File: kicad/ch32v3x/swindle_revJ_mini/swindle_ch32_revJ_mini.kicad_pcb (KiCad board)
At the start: 2 copper layers, 49.8 x 33.3 mm, 65 parts, among them J1 jtag, J10 Debug port, J2 Conn_01x03_Socket, J2_DFU1 con2, J3 Dbg, J4 USB, J5 Debug port, J6 Debug port, J7 Conn_01x03_Pin, J8 Debug port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

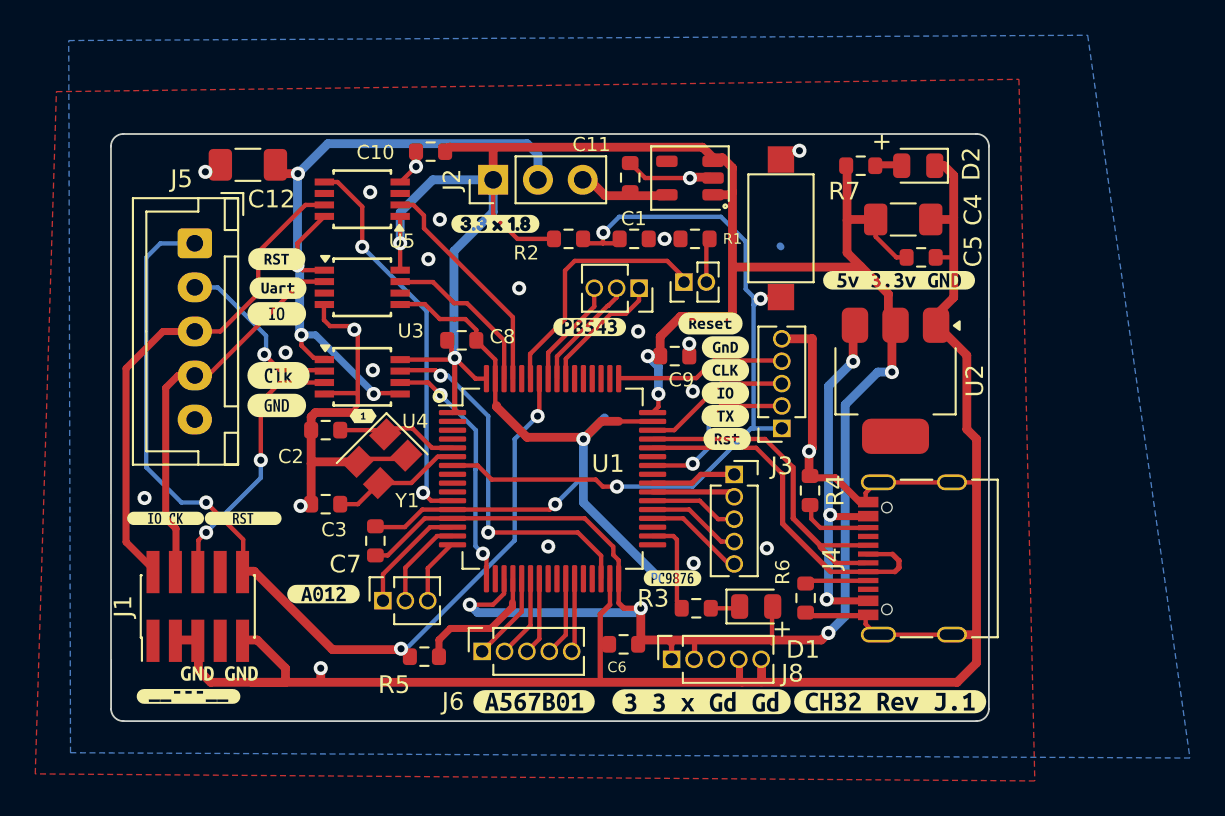
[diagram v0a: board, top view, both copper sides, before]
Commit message: add a WS2812b to the mini version, mini version for CH32,GD32 and RP2xxx
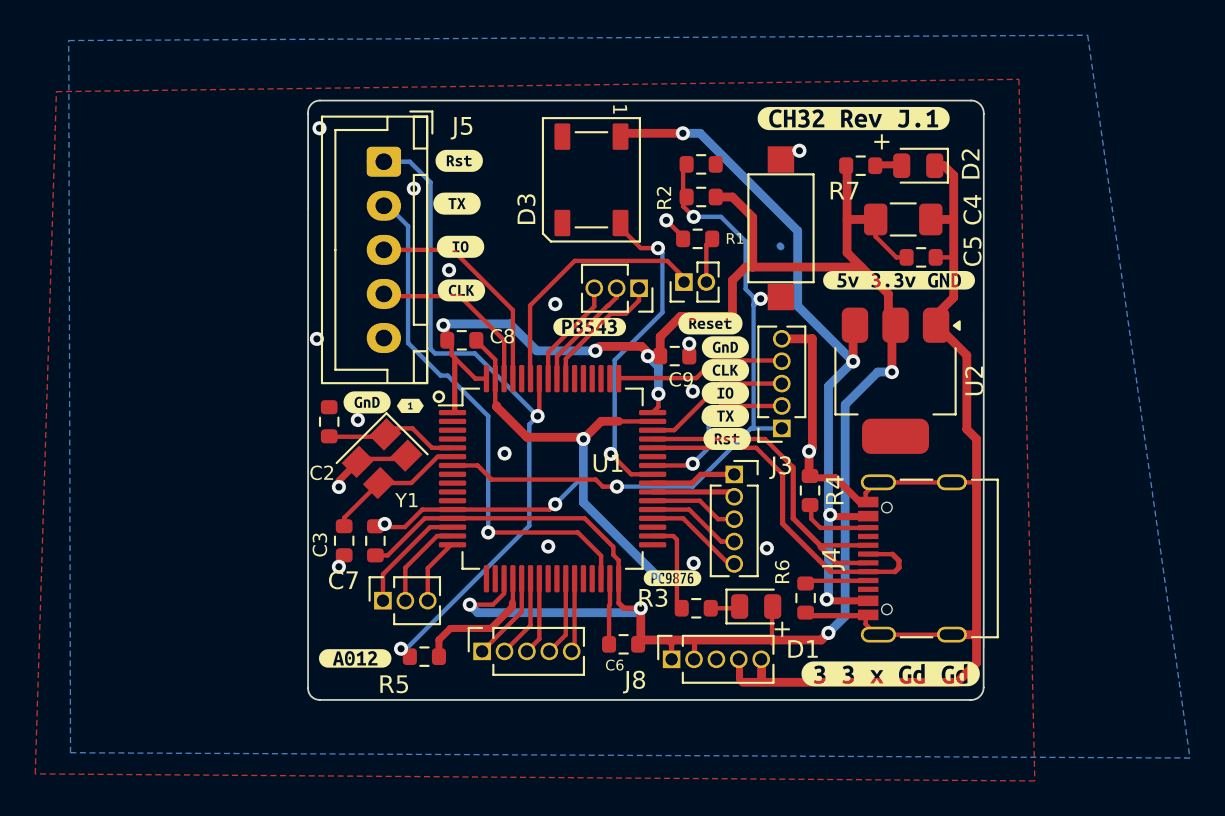
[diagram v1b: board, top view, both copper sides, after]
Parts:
- removed C10, C11: 100n, Resistor_SMD:R_0603_1608Metric
- removed C12: 100u, Capacitor_SMD:C_1206_3216Metric_Pad1.33x1.80mm_HandSolder
- removed J1: jtag, Connector_PinHeader_1.27mm:PinHeader_2x05_P1.27mm_Vertical_SMD
- removed J2: Conn_01x03_Socket, Connector_PinHeader_2.54mm:PinHeader_1x03_P2.54mm_Vertical
- removed U3: 3V->VTREF, Package_SO:TSSOP-8_3x3mm_P0.65mm
- removed U4: VTREF->3V, Package_SO:TSSOP-8_3x3mm_P0.65mm
- removed U5: VTREF<->3V, Package_SO:TSSOP-8_3x3mm_P0.65mm
- removed U6: RT9013-33GB, PCM_Package_TO_SOT_SMD_AKL:TSOT-23-5
- removed kibuzzard-66C04372: G***, kibuzzard-66C04372
- removed kibuzzard-66C0437E: G***, kibuzzard-66C0437E
- removed kibuzzard-67135DB6: G***, kibuzzard-67135DB6
- removed kibuzzard-67137B47: G***, kibuzzard-67137B47
- removed kibuzzard-67137B7B: G***, kibuzzard-67137B7B
- removed kibuzzard-6713DC16: G***, kibuzzard-6713DC16
- removed kibuzzard-6713DC2E: G***, kibuzzard-6713DC2E
- removed kibuzzard-6714FCCA: G***, kibuzzard-6714FCCA
- removed kibuzzard-6714FD27: G***, kibuzzard-6714FD27
- removed kibuzzard-6731069B: G***, kibuzzard-6731069B
- removed kibuzzard-67310708: G***, kibuzzard-67310708
- removed kibuzzard-6731071F: G***, kibuzzard-6731071F
- added D3: WS2812B, LED_SMD:LED_WS2812B_PLCC4_5.0x5.0mm_P3.2mm, F.Cu at (132.8, 69.5)
- added kibuzzard-65C1C789: G***, kibuzzard-65C1C789, F.Cu at (120.0, 82.1)
- added kibuzzard-65C1C8EE: G***, kibuzzard-65C1C8EE, F.Cu at (125.4, 75.8)
- added kibuzzard-65C1C918: G***, kibuzzard-65C1C918, F.Cu at (125.3, 73.3)
- added kibuzzard-65C1C92F: G***, kibuzzard-65C1C92F, F.Cu at (125.1, 70.8)
- added kibuzzard-65C1C972: G***, kibuzzard-65C1C972, F.Cu at (125.3, 68.4)
- moved kibuzzard-6869421E 33.1 mm to (147.6, 66.0)
- moved J5 11.7 mm to (121.0, 68.5)
- moved kibuzzard-6714FD4B 10.8 mm to (149.7, 97.5)
- moved R2 7.89 mm to (139.0, 70.5), turned to 180 degrees
- moved C1 5.68 mm to (139.0, 68.6)
- moved kibuzzard-67135D9A 4.07 mm to (119.4, 96.6)
- moved kibuzzard-671361D3 2.74 mm to (122.5, 82.3)
- moved C3 2.33 mm to (118.7, 90.0), turned to -90 degrees
- moved C2 0.52 mm to (117.9, 83.2), turned to 90 degrees
- moved R1 0.15 mm to (138.8, 72.8)
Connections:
- net Net-(U2-VI) renamed VBUS
- U1 pad 17: INOUT_SWO_3v -> INOUT_SWO
- U1 pad 30: OUT_UART_RX_3V -> OUT_UART_RX
- U1 pad 41: unconnected-(U1-PA8-Pad41) -> PA8
- U1 pad 61: OUT_SWDIO_3V -> OUT_SWDIO
- U1 pad 62: OUT_SWDCLK_3V -> OUT_SWDCLK
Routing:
- net GND: track 200.5 -> 126.3 mm, vias 24 -> 20
- net VTREF: track 40.3 -> 0.00 mm, vias 4 -> 0
- net +3.3V: track 163.6 -> 126.9 mm
- net SWIO_DIR_3V: track 22.5 -> 0.00 mm, vias 2 -> 0
- net OUT_UART_RX_3V: track 21.1 -> 0.00 mm, vias 2 -> 0
- net VBUS: track 20.5 -> 41.4 mm, vias 3 -> 4
- net OUT_UART_RX: track 10.4 -> 29.1 mm
- net PA8: track 0.00 -> 18.4 mm, vias 0 -> 2
- net OUT_SWDIO: track 28.9 -> 12.6 mm
- net INOUT_SWO: track 15.4 -> 0.00 mm, vias 2 -> 0
- net INOUT_SWO_3v: track 14.4 -> 0.00 mm, vias 2 -> 0
- net INOUT_NRESET: track 53.6 -> 39.8 mm, vias 3 -> 2
- net OUT_SWDIO_3V: track 12.9 -> 0.00 mm
- net OUT_SWDCLK: track 22.1 -> 9.91 mm
- net OUT_SWDCLK_3V: track 9.50 -> 0.00 mm
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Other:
- board size 49.8 x 33.3 mm -> 38.3 x 34 mm

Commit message: kicad: order to pcbway
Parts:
- added C10: 100n, Resistor_SMD:R_0603_1608Metric, F.Cu at (136.6, 68.0)
- added Q1: DMG2302U, Package_TO_SOT_SMD:SOT-23, F.Cu at (127.9, 67.5)
- added R8: 330, Resistor_SMD:R_0603_1608Metric, F.Cu at (125.0, 67.0)
- added R9: 1k, Resistor_SMD:R_0603_1608Metric, F.Cu at (128.6, 72.4)
- moved kibuzzard-65C1C972 1.62 mm to (125.3, 70.0)
- moved kibuzzard-65C1C92F 1.43 mm to (125.3, 72.3)
- moved kibuzzard-65C1C918 0.25 mm to (125.4, 73.5)
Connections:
- D3 pad 4: PA8 -> PB4
- U1 pad 58: INOUT_NRESET -> DRIVE_RESET
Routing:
- net PA8: track 18.4 -> 0.00 mm, vias 2 -> 0
- net DRIVE_RESET: track 0.00 -> 13.8 mm, vias 0 -> 2
- net PB4: track 6.55 -> 12.7 mm, vias 0 -> 1
- net Net-(Q1-D): track 0.00 -> 3.02 mm
- net INOUT_NRESET: track 39.8 -> 41.9 mm, vias 2 -> 1
- net GND: track 126.3 -> 127.1 mm, vias 20 -> 21

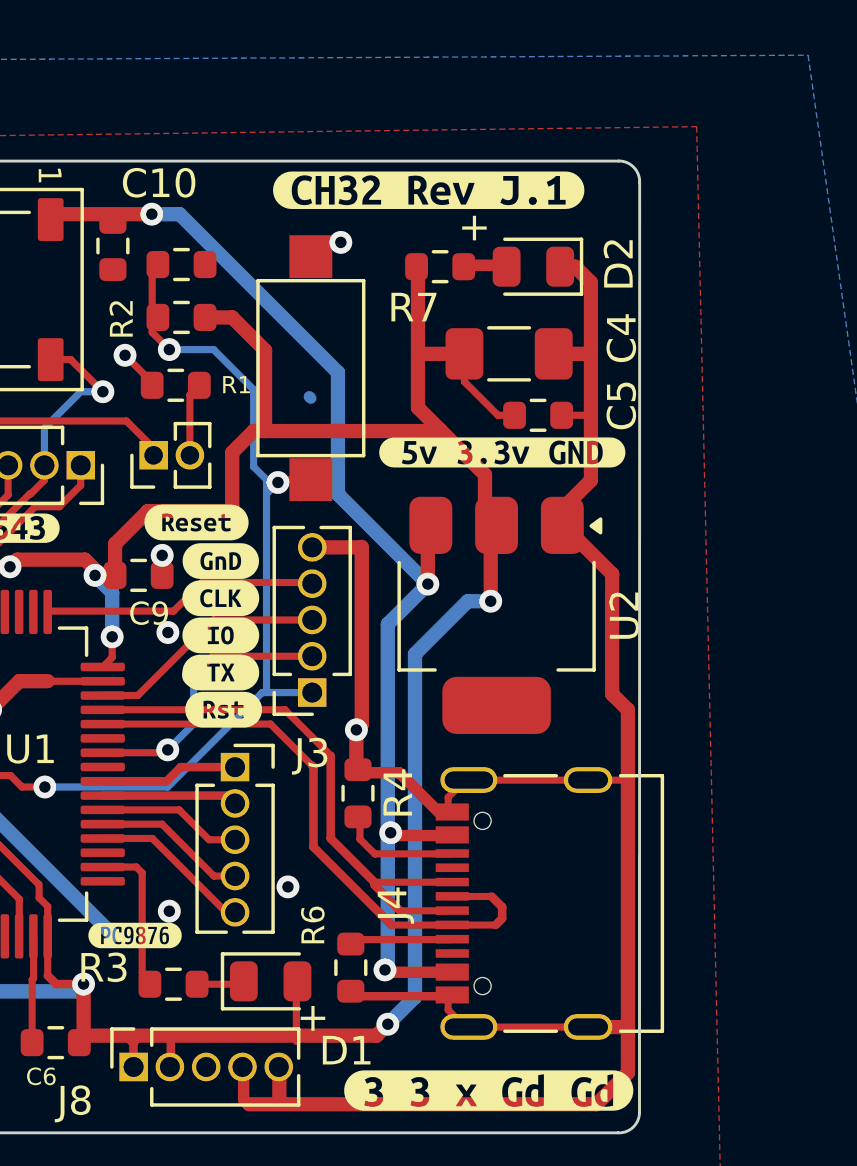
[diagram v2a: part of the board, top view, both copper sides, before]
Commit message: Kicad : ch32v3, add a (optional) 1.2k pullup on D+ so it can be used for GD32F303/64pins package
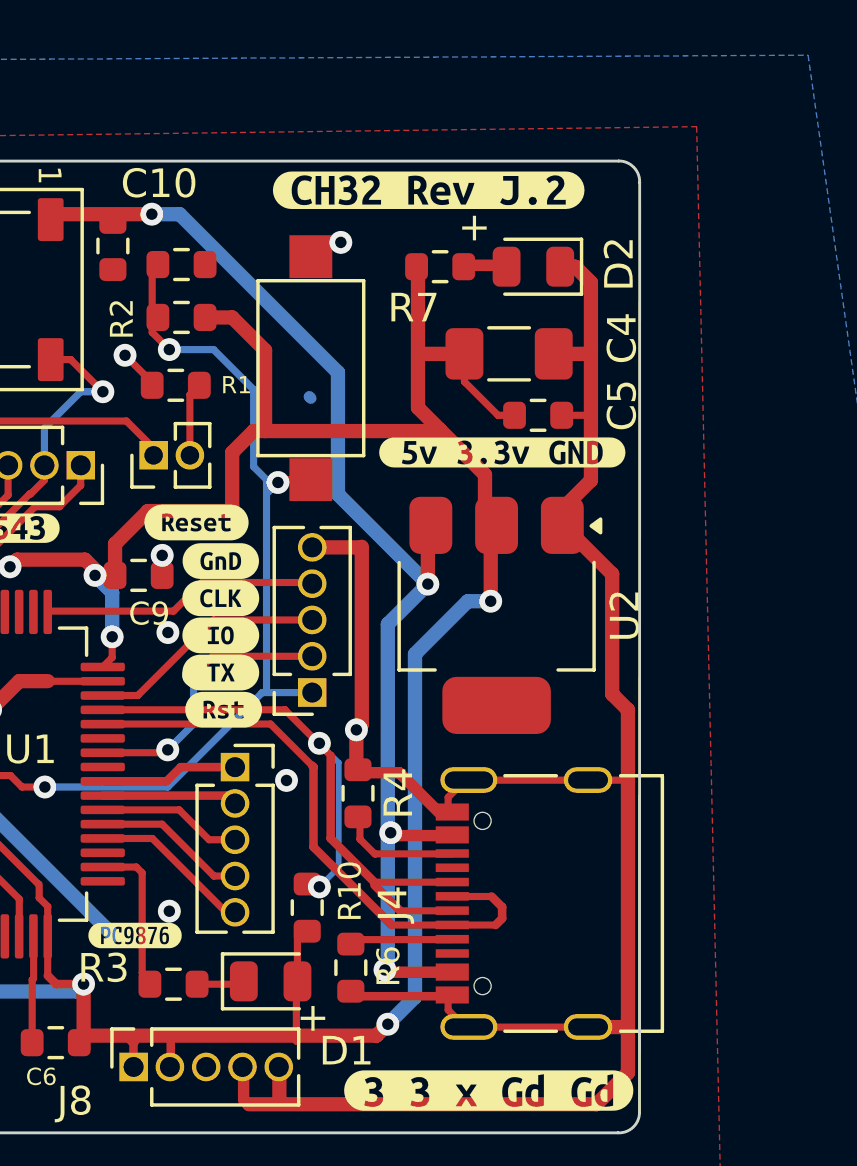
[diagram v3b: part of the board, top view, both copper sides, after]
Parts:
- removed kibuzzard-6869421E: G***, kibuzzard-6869421E
- added R10: 1.2k, Resistor_SMD:R_0603_1608Metric, F.Cu at (143.4, 91.1)
- added kibuzzard-68977CD7: G***, kibuzzard-68977CD7, F.Cu at (147.6, 66.0)
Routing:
- net D+: track 19.3 -> 24.9 mm, vias 0 -> 2
- net +3.3V: track 126.9 -> 129.0 mm

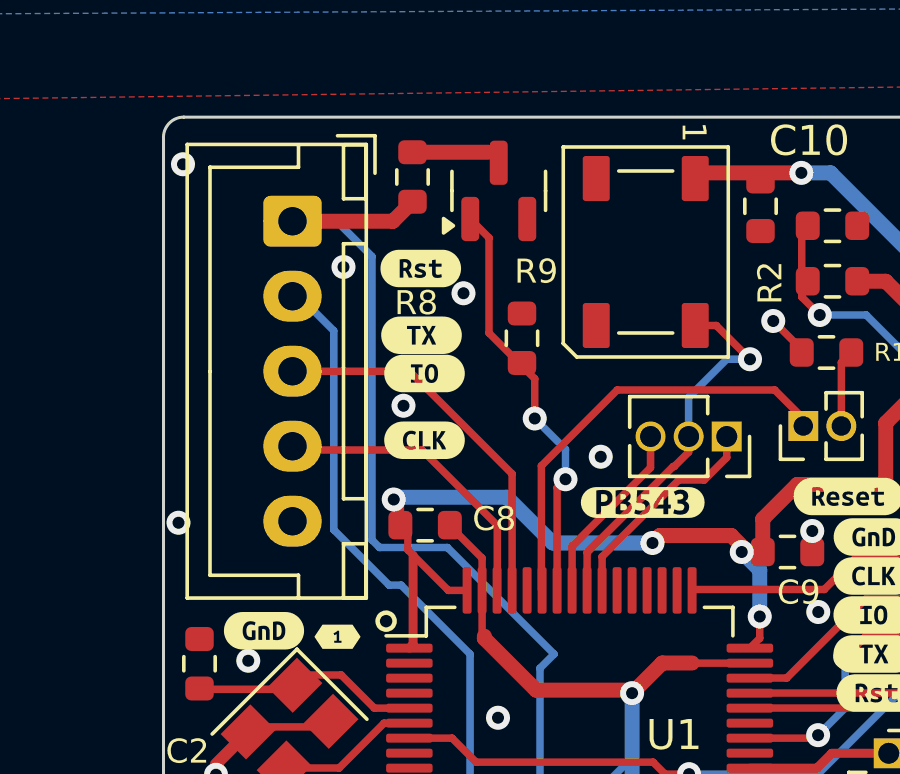
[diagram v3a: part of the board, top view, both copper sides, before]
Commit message: kicad/ch32 mini : fix boot0
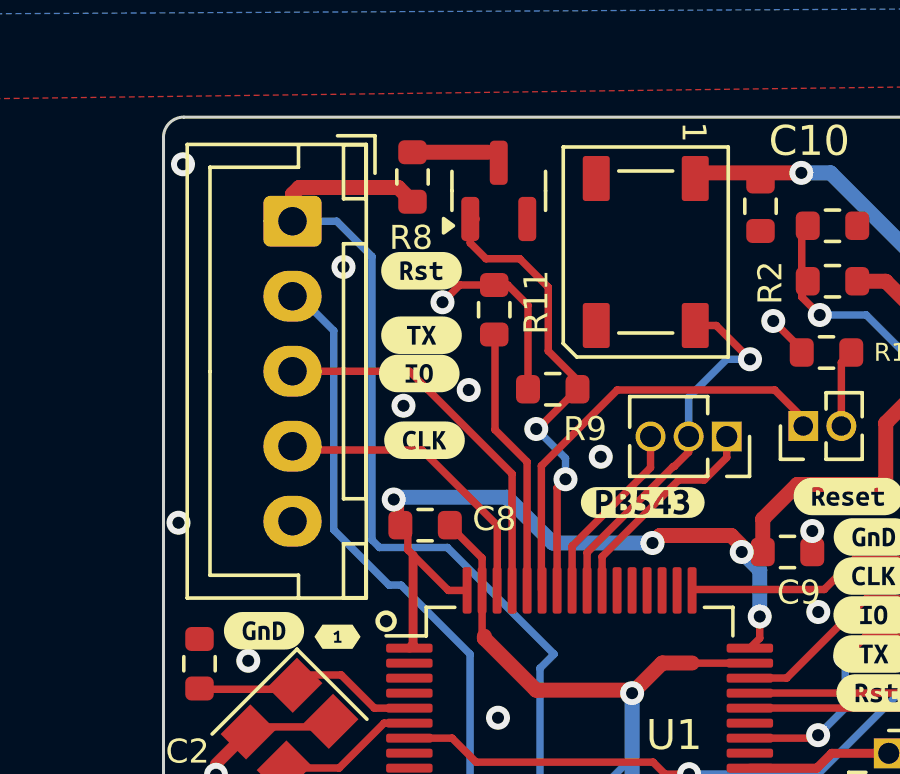
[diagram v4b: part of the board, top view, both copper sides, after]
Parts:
- added R11: 1k, Resistor_SMD:R_0603_1608Metric, F.Cu at (127.7, 71.4)
- moved R9 1.99 mm to (129.7, 74.1), turned to 180 degrees
- moved kibuzzard-65C1C918 0.17 mm to (125.2, 73.5)
- moved kibuzzard-65C1C972 0.08 mm to (125.3, 70.1)
- renumbered Q1 to Q1-A2SHB1
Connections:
- U1 pad 60: unconnected-(U1-BOOT0-Pad60) -> Net-(U1-BOOT0)
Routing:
- net Net-(U1-BOOT0): track 0.00 -> 8.75 mm
- net GND: track 127.1 -> 133.2 mm, vias 21 -> 22
- net DRIVE_RESET: track 13.8 -> 15.8 mm
- net INOUT_NRESET: track 41.9 -> 42.9 mm
